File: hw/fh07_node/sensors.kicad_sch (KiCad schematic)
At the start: 0 parts

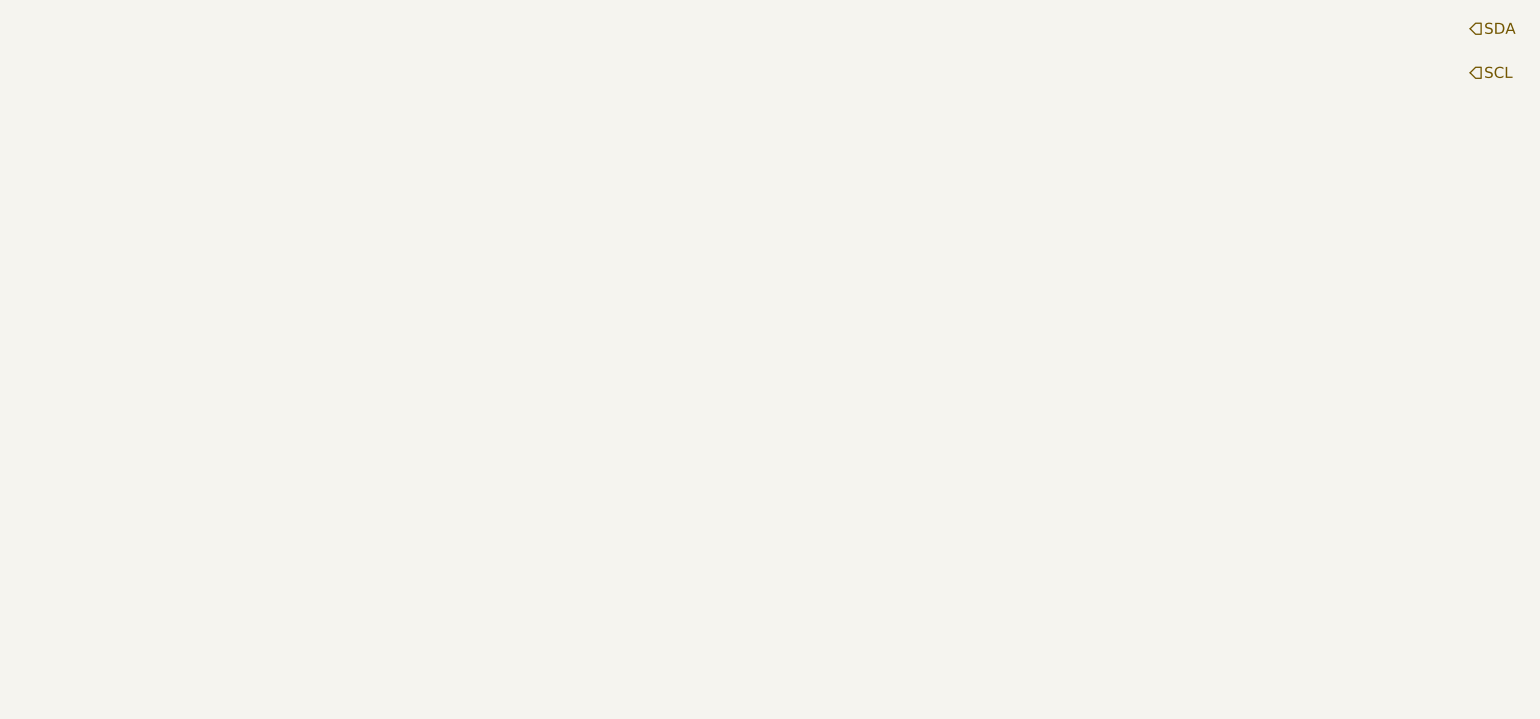
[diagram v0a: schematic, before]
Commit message: Add IMU and magnetometer schematics and libraries
- Added ICM-42670-P IMU schematic
- Added BMM350 magnetometer schematic
- Added symbols, footprints, and 3D models to repo libraries
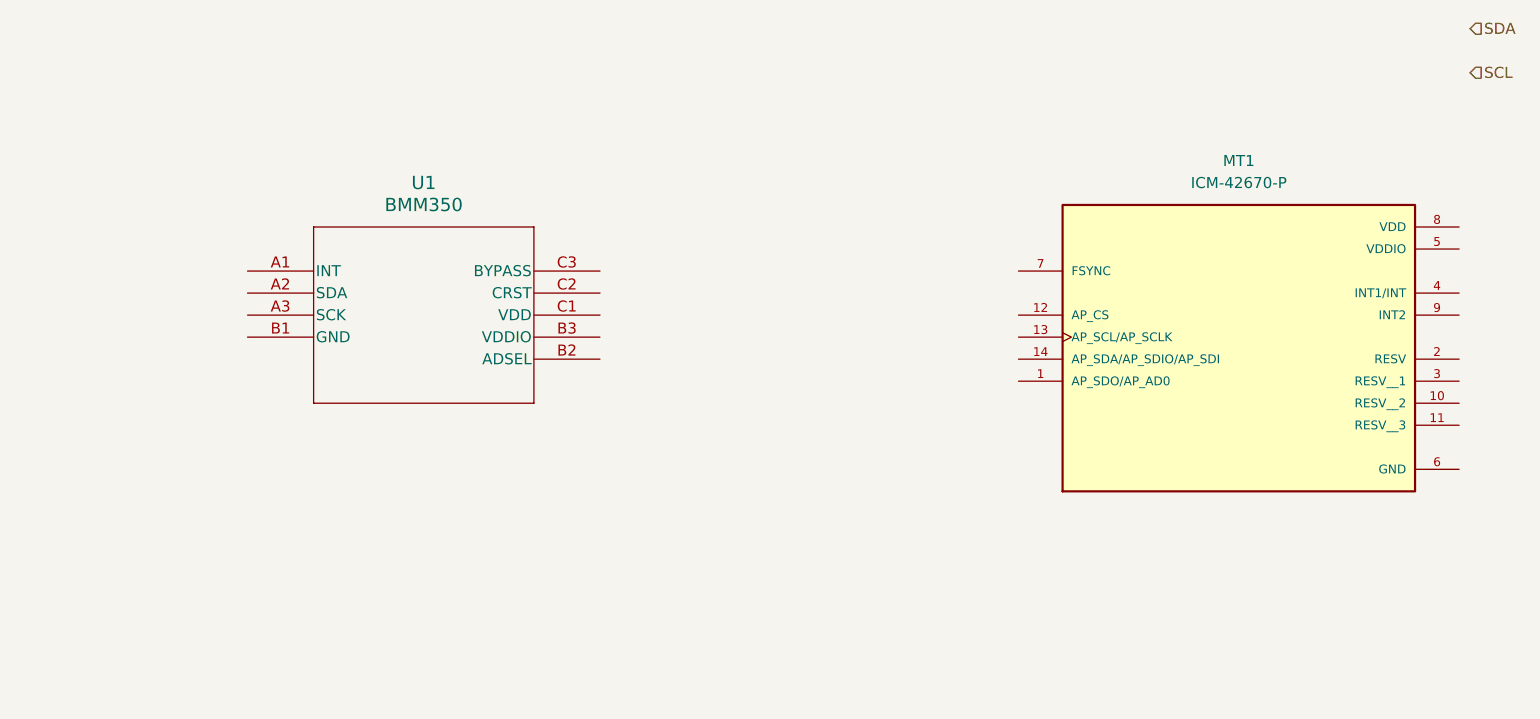
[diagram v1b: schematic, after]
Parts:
- added MT1: ICM-42670-P, ICM-42670-P:XDCR_ICM-42670-P, symbol ICM-42670-P:ICM-42670-P
- added U1: BMM350, BGA9_BMM350_BOS, symbol 2026-02-07_18-33-16:BMM350
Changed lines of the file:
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@@
 		)
 	)
+	(symbol
+		(lib_id "ICM-42670-P:ICM-42670-P")
+		(at 179.07 83.82 0)
+		(unit 1)
+		(exclude_from_sim no)
+		(in_bom yes)
+		(on_board yes)
+		(dnp no)
+		(fields_autoplaced yes)
+		(property "Reference" "MT1"
+			(at 179.07 66.04 0)
+			(effects
+				(font
+					(size 1.27 1.27)
+				)
+			)
+		)
+		(property "Value" "ICM-42670-P"
+			(at 179.07 68.58 0)
+			(effects
+				(font
+					(size 1.27 1.27)
+				)
+			)
+		)
+		(property "Footprint" "ICM-42670-P:XDCR_ICM-42670-P"
+			(at 179.07 83.82 0)
+			(effects
+				(font
+					(size 1.27 1.27)
+				)
+				(justify bottom)
+				(hide yes)
+			)
+		)
+		(property "Datasheet" ""
+			(at 179.07 83.82 0)
+			(effects
+				(font
+					(size 1.27 1.27)
+				)
+				(hide yes)
+			)
+		)
+		(property "Description" ""
+			(at 179.07 83.82 0)
+			(effects
+				(font
+					(size 1.27 1.27)
+				)
+				(hide yes)
+			)
+		)
+		(property "PARTREV" "1.1"
+			(at 179.07 83.82 0)
+			(effects
+				(font
+					(size 1.27 1.27)
+				)
+				(justify bottom)
+				(hide yes)
+			)
+		)
+		(property "STANDARD" "Manufacturer Recommendations"
+			(at 179.07 83.82 0)
+			(effects
+				(font
+					(size 1.27 1.27)
+				)
+				(justify bottom)
+				(hide yes)
+			)
+		)
+		(property "MAXIMUM_PACKAGE_HEIGHT" "0.81 mm"
+			(at 179.07 83.82 0)
+			(effects
+				(font
+					(size 1.27 1.27)
+				)
+				(justify bottom)
+				(hide yes)
+			)
+		)
+		(property "MANUFACTURER" "TDK InvenSense"
+			(at 179.07 83.82 0)
+			(effects
+				(font
+					(size 1.27 1.27)
+				)
+				(justify bottom)
+				(hide yes)
+			)
+		)
+		(pin "8"
+		)
+		(pin "9"
+		)
+		(pin "10"
+		)
+		(pin "3"
+		)
+		(pin "2"
+		)
+		(pin "11"
+		)
+		(pin "12"
+		)
+		(pin "7"
+		)
+		(pin "14"
+		)
+		(pin "1"
+		)
+		(pin "13"
+		)
+		(pin "5"
+		)
+		(pin "4"
+		)
+		(pin "6"
+		)
+		(instances
+			(project ""
+				(path "/62bb0011-0a7e-4eb0-868e-e75c2c4b5ec3"
+					(reference "MT1")
+					(unit 1)
+				)
+			)
+		)
+	)
+	(symbol
+		(lib_id "2026-02-07_18-33-16:BMM350")
+		(at 64.77 78.74 0)
+		(unit 1)
+		(exclude_from_sim no)
+		(in_bom yes)
+		(on_board yes)
+		(dnp no)
+		(fields_autoplaced yes)
+		(property "Reference" "U1"
+			(at 85.09 68.58 0)
+			(effects
+				(font
+					(size 1.524 1.524)
+				)
+			)
+		)
+		(property "Value" "BMM350"
+			(at 85.09 71.12 0)
+			(effects
+				(font
+					(size 1.524 1.524)
+				)
+			)
+		)
+		(property "Footprint" "BGA9_BMM350_BOS"
+			(at 64.77 78.74 0)
+			(effects
+				(font
+					(size 1.27 1.27)
+					(italic yes)
+				)
+				(hide yes)
+			)
+		)
+		(property "Datasheet" "BMM350"
+			(at 64.77 78.74 0)
+			(effects
+				(font
+					(size 1.27 1.27)
+					(italic yes)
+				)
+				(hide yes)
+			)
+		)
+		(property "Description" ""
+			(at 64.77 78.74 0)
+			(effects
+				(font
+					(size 1.27 1.27)
+				)
+				(hide yes)
+			)
+		)
+		(pin "C1"
+		)
+		(pin "C3"
+		)
+		(pin "A1"
+		)
+		(pin "A2"
+		)
+		(pin "C2"
+		)
+		(pin "B3"
+		)
+		(pin "A3"
+		)
+		(pin "B2"
+		)
+		(pin "B1"
+		)
+		(instances
+			(project ""
+				(path "/62bb0011-0a7e-4eb0-868e-e75c2c4b5ec3"
+					(reference "U1")
+					(unit 1)
+				)
+			)
+		)
+	)
+	(sheet_instances
+		(path "/"
+			(page "1")
+		)
+	)
+	(embedded_fonts no)
 )

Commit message: Pushed updates to hardware
Completed sensors.kicad_sch

Added BNO055 symbol and footprint files to Part_Libraries

Added I²C pull-ups, reset circuitry, and required decoupling components

Followed the BNO055 connection diagram from the datasheet for wiring
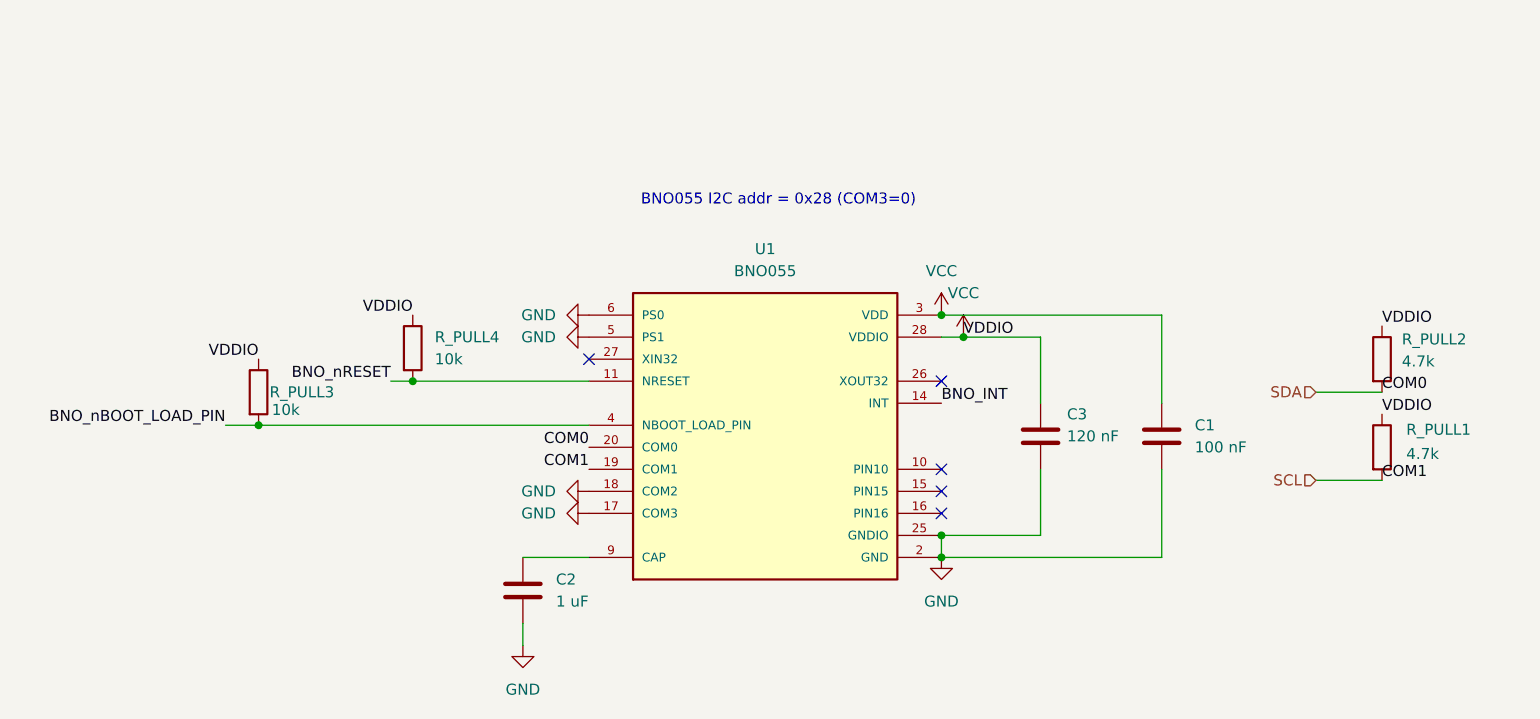
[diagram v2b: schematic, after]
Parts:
- removed MT1: ICM-42670-P, ICM-42670-P:XDCR_ICM-42670-P, symbol ICM-42670-P:ICM-42670-P
- removed U1: BMM350, BGA9_BMM350_BOS, symbol 2026-02-07_18-33-16:BMM350
- added C1: 100 nF, symbol Device:C
- added C2: 1 uF, symbol Device:C
- added C3: 120 nF, symbol Device:C
- added R_PULL1, R_PULL2: 4.7k, symbol Device:R
- added R_PULL3, R_PULL4: 10k, symbol Device:R
- added U1: BNO055, BNO055:LGA28R50P4X10_380X520X100, symbol BNO055:BNO055
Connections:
- net SCL: now also R_PULL1.2, U1.19 (COM1)
- net SDA: now also R_PULL2.2, U1.20 (COM0)
- new net: C2.1, U1.9 (CAP)
- new net BNO_INT: U1.14 (INT)
- new net BNO_nBOOT_LOAD_PIN: R_PULL3.2, U1.4 (NBOOT_LOAD_PIN)
- new net BNO_nRESET: R_PULL4.2, U1.11 (NRESET)
- new net GND: C1.2, C2.2, C3.2, U1.17 (COM3), U1.18 (COM2), U1.2 (GND), U1.25 (GNDIO), U1.5 (PS1), U1.6 (PS0)
- new net VCC: C1.1, C3.1, R_PULL1.1, R_PULL2.1, R_PULL3.1, R_PULL4.1, U1.28 (VDDIO), U1.3 (VDD)
- no-connect marks 0 -> 5
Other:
- note added: "BNO055 I2C addr = 0x28 (COM3=0)"

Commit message: Updated sensor node and top level sheet
Fixed pin naming on sensor module and update MCU and Sensor top sheet
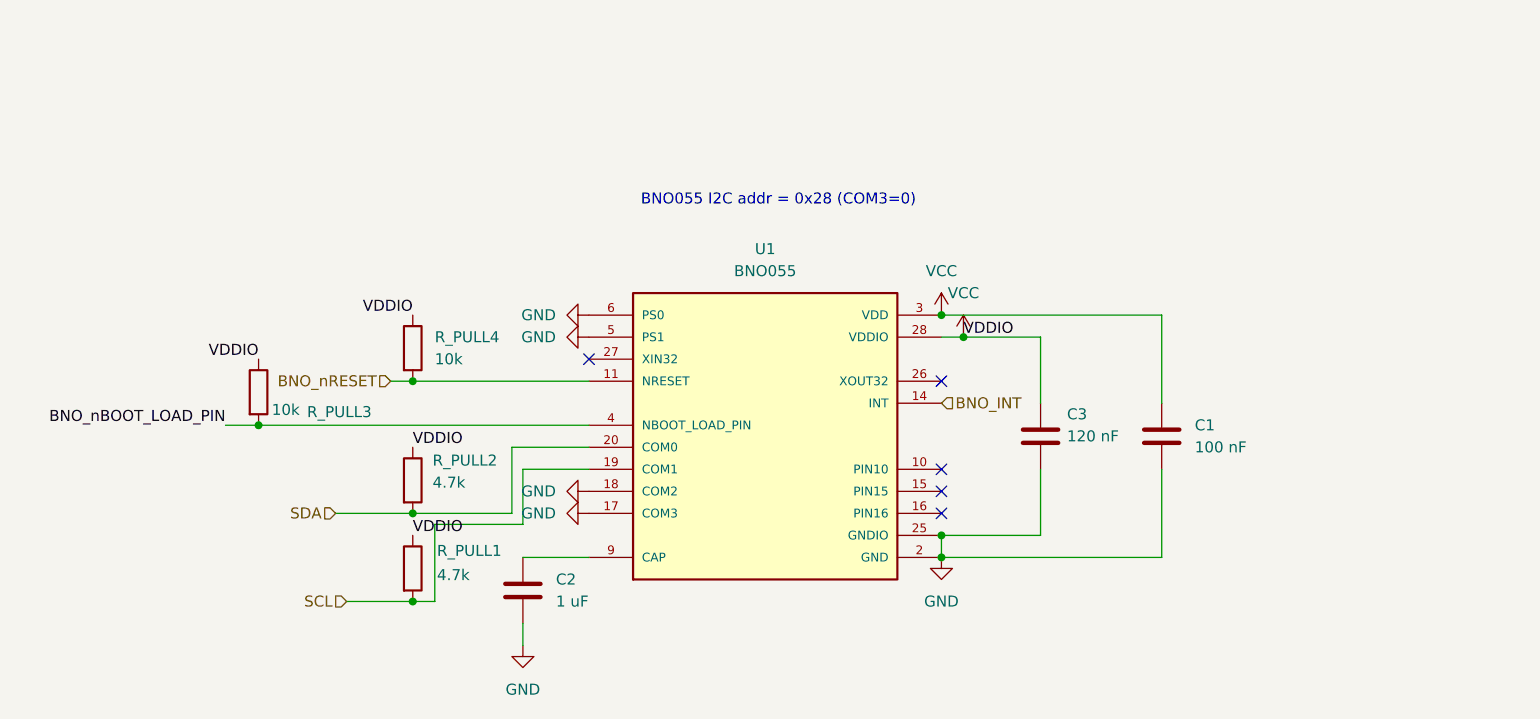
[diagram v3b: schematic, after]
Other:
- moved on the sheet: R_PULL1, R_PULL2
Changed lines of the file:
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@@
+	)
+	(junction
+		(at 83.82 116.84)
+		(diameter 0)
+		(color 0 0 0 0)
 	)
 	(junction
@@
 	)
 	(junction
+		(at 83.82 106.68)
+		(diameter 0)
+		(color 0 0 0 0)
+	)
+	(junction
 		(at 66.04 96.52)
 		(diameter 0)
@@
 	(wire
 		(pts
+			(xy 104.14 101.6) (xy 96.52 101.6)
+		)
+		(stroke
+			(width 0)
+			(type default)
+		)
+	)
+	(wire
+		(pts
 			(xy 144.78 86.36) (xy 147.32 86.36)
 		)
@@
 	(wire
 		(pts
+			(xy 96.52 107.95) (xy 86.36 107.95)
+		)
+		(stroke
+			(width 0)
+			(type default)
+		)
+	)
+	(wire
+		(pts
 			(xy 66.04 96.52) (xy 104.14 96.52)
 		)
@@
 	(wire
 		(pts
-			(xy 187.96 102.87) (xy 195.58 102.87)
+			(xy 76.2 116.84) (xy 83.82 116.84)
 		)
 		(stroke
@@
 	(wire
 		(pts
-			(xy 187.96 92.71) (xy 195.58 92.71)
+			(xy 74.93 106.68) (xy 83.82 106.68)
+		)
+		(stroke
+			(width 0)
+			(type default)
+		)
+	)
+	(wire
+		(pts
+			(xy 86.36 116.84) (xy 83.82 116.84)
 		)
 		(stroke
@@
 	(wire
 		(pts
+			(xy 86.36 107.95) (xy 86.36 116.84)
+		)
+		(stroke
+			(width 0)
+			(type default)
+		)
+	)
+	(wire
+		(pts
 			(xy 156.21 101.6) (xy 156.21 109.22)
 		)
@@
 	(wire
 		(pts
+			(xy 104.14 99.06) (xy 95.25 99.06)
+		)
+		(stroke
+			(width 0)
+			(type default)
+		)
+	)
+	(wire
+		(pts
+			(xy 95.25 106.68) (xy 83.82 106.68)
+		)
+		(stroke
+			(width 0)
+			(type default)
+		)
+	)
+	(wire
+		(pts
+			(xy 95.25 99.06) (xy 95.25 106.68)
+		)
+		(stroke
+			(width 0)
+			(type default)
+		)
+	)
+	(wire
+		(pts
+			(xy 96.52 101.6) (xy 96.52 107.95)
+		)
+		(stroke
+			(width 0)
+			(type default)
+		)
+	)
+	(wire
+		(pts
 			(xy 156.21 109.22) (xy 144.78 109.22)
 		)
@@
 			(width 0)
 			(type default)
-		)
-	)
-	(label "BNO_INT"
-		(at 144.78 93.98 0)
-		(effects
-			(font
-				(size 1.27 1.27)
-			)
-			(justify left bottom)
 		)
 	)
@@
 		)
 	)
-	(label "COM0"
-		(at 195.58 92.71 0)
-		(effects
-			(font
-				(size 1.27 1.27)
-			)
-			(justify left bottom)
-		)
-	)
 	(label "VDDIO"
 		(at 83.82 83.82 180)
@@
 		)
 	)
-	(label "COM0"
-		(at 104.14 99.06 180)
-		(effects
-			(font
-				(size 1.27 1.27)
-			)
-			(justify right bottom)
-		)
-	)
 	(label "VDDIO"
-		(at 195.58 95.25 0)
+		(at 83.82 109.22 0)
 		(effects
 			(font
@@
 			)
 			(justify left bottom)
-		)
-	)
-	(label "COM1"
-		(at 104.14 101.6 180)
-		(effects
-			(font
-				(size 1.27 1.27)
-			)
-			(justify right bottom)
-		)
-	)
-	(label "BNO_nRESET"
-		(at 81.28 91.44 180)
-		(effects
-			(font
-				(size 1.27 1.27)
-			)
-			(justify right bottom)
 		)
 	)
@@
 	)
 	(label "VDDIO"
-		(at 195.58 85.09 0)
+		(at 83.82 99.06 0)
 		(effects
 			(font
@@
 		)
 	)
-	(label "COM1"
-		(at 195.58 102.87 0)
-		(effects
-			(font
-				(size 1.27 1.27)
-			)
-			(justify left bottom)
+	(hierarchical_label "BNO_INT"
+		(shape input)
+		(at 144.78 93.98 0)
+		(effects
+			(font
+				(size 1.27 1.27)
+			)
+			(justify left)
 		)
 	)
 	(hierarchical_label "SCL"
 		(shape input)
-		(at 187.96 102.87 180)
+		(at 76.2 116.84 180)
 		(effects
 			(font
@@
 	(hierarchical_label "SDA"
 		(shape input)
-		(at 187.96 92.71 180)
+		(at 74.93 106.68 180)
+		(effects
+			(font
+				(size 1.27 1.27)
+			)
+			(justify right)
+		)
+	)
+	(hierarchical_label "BNO_nRESET"
+		(shape input)
+		(at 81.28 91.44 180)
 		(effects
 			(font
@@
 	(symbol
 		(lib_id "Device:R")
-		(at 195.58 99.06 0)
+		(at 83.82 113.03 0)
 		(unit 1)
 		(exclude_from_sim no)
@@
 		(dnp no)
 		(property "Reference" "R_PULL1"
-			(at 198.374 97.028 0)
+			(at 86.614 110.998 0)
 			(effects
 				(font
@@
 		)
 		(property "Value" "4.7k"
-			(at 198.374 99.822 0)
+			(at 86.614 113.792 0)
 			(effects
 				(font
@@
 		)
 		(property "Footprint" ""
-			(at 193.802 99.06 90)
+			(at 82.042 113.03 90)
 			(effects
 				(font
@@
 		)
 		(property "Datasheet" "~"
-			(at 195.58 99.06 0)
+			(at 83.82 113.03 0)
 			(effects
 				(font
@@
 		)
 		(property "Description" "Resistor"
-			(at 195.58 99.06 0)
+			(at 83.82 113.03 0)
 			(effects
 				(font
@@
 	(symbol
 		(lib_id "Device:R")
-		(at 195.58 88.9 0)
+		(at 83.82 102.87 0)
 		(unit 1)
 		(exclude_from_sim no)
@@
 		(dnp no)
 		(property "Reference" "R_PULL2"
-			(at 197.866 86.614 0)
+			(at 86.106 100.584 0)
 			(effects
 				(font
@@
 		)
 		(property "Value" "4.7k"
-			(at 197.866 89.154 0)
+			(at 86.106 103.124 0)
 			(effects
 				(font
@@
 		)
 		(property "Footprint" ""
-			(at 193.802 88.9 90)
+			(at 82.042 102.87 90)
 			(effects
 				(font
@@
 		)
 		(property "Datasheet" "~"
-			(at 195.58 88.9 0)
+			(at 83.82 102.87 0)
 			(effects
 				(font
@@
 		)
 		(property "Description" "Resistor"
-			(at 195.58 88.9 0)
+			(at 83.82 102.87 0)
 			(effects
 				(font
@@
 		(dnp no)
 		(property "Reference" "R_PULL3"
-			(at 67.31 92.71 0)
-			(effects
-				(font
+			(at 71.628 94.996 0)
+			(effects
+				(font

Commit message: New KiCad version test
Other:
- note added: "BNO055 I2C addr = 0x28 (COM3=0)."
- note removed: "BNO055 I2C addr = 0x28 (COM3=0)"
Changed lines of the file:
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@@
 		(date "2026-02-04")
 	)
-	(text "BNO055 I2C addr = 0x28 (COM3=0)"
+	(text "BNO055 I2C addr = 0x28 (COM3=0)."
 		(exclude_from_sim no)
 		(at 125.984 70.612 0)
